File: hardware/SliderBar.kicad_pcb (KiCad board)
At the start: 2 copper layers, 36 parts, among them J1 USB_B_Mini, J2 MOTOR_OUT, J3 POT_IN, J4 DEBUG, U1 MIC5205-3.3YM5, U2 MT3608, U3 STM32F072C8Tx, U4 TB6612FNG

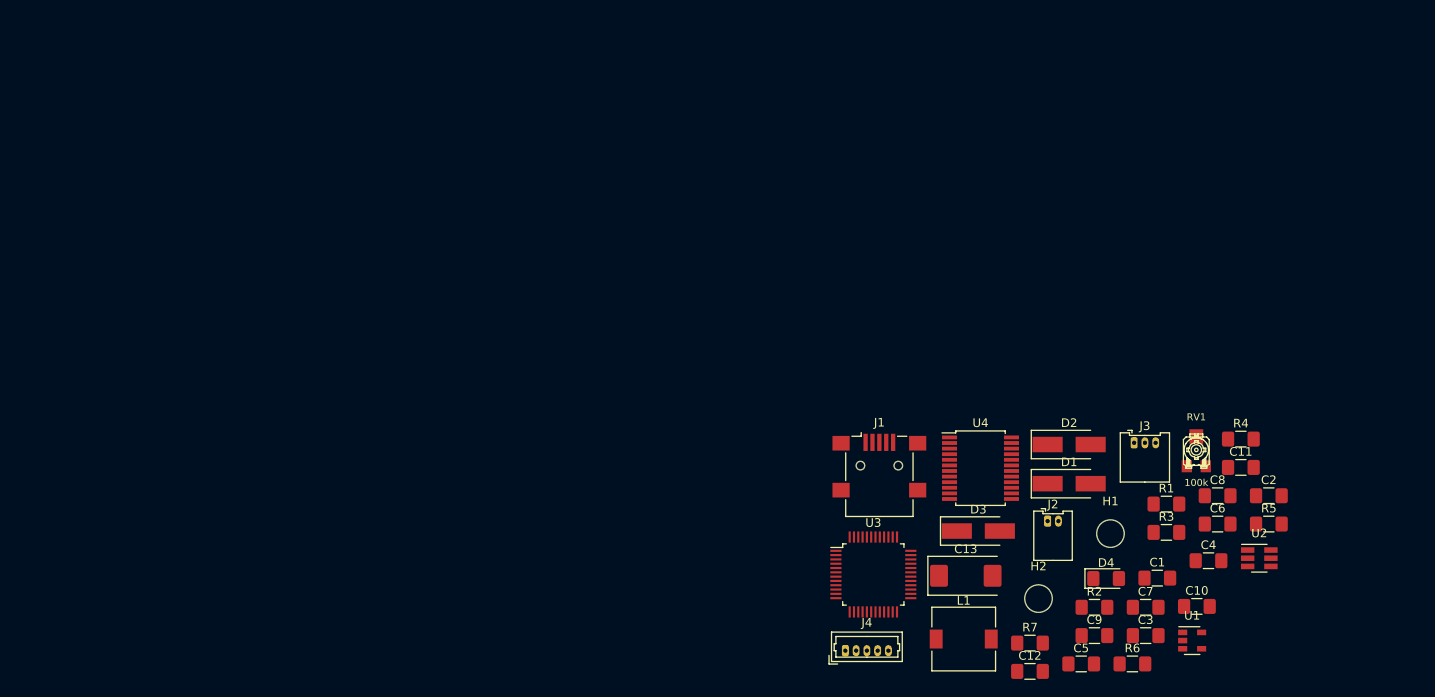
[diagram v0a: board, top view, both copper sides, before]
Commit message: Fix potentiometer wiring, move Nelib library outside of project
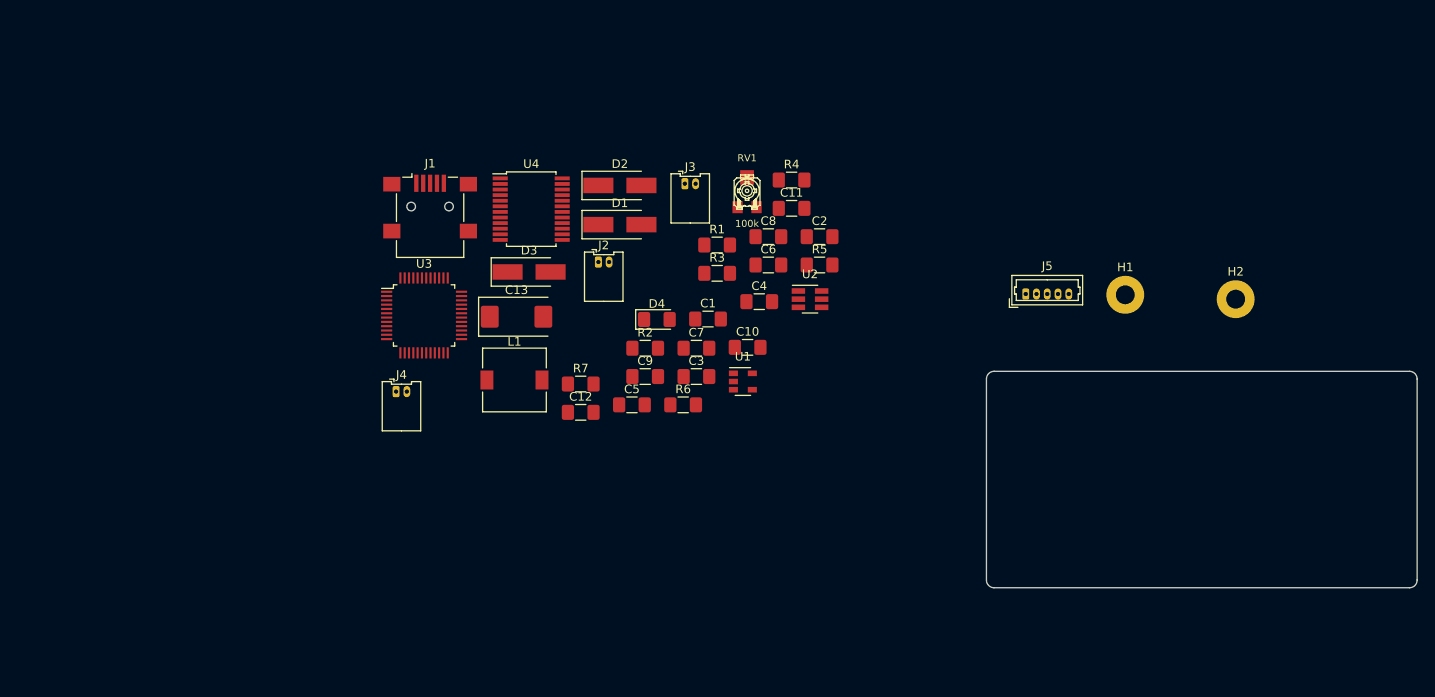
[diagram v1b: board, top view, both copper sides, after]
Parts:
- added J5: DEBUG, Connector_Molex:Molex_PicoBlade_53047-0510_1x05_P1.25mm_Vertical, F.Cu at (141.9, 46.9)
- H1, H2: footprint MountingHole:MountingHole_3.2mm_M3_ISO14580 -> MountingHole:MountingHole_2.2mm_M2_Pad
- J2: value MOTOR_OUT -> MOTOR
- J3: value POT_IN -> TAPER_RIGHT; footprint Connector_Molex:Molex_PicoBlade_53048-0310_1x03_P1.25mm_Horizontal -> Connector_Molex:Molex_PicoBlade_53048-0210_1x02_P1.25mm_Horizontal
- J4: value DEBUG -> TAPER_LEFT; footprint Connector_Molex:Molex_PicoBlade_53047-0510_1x05_P1.25mm_Vertical -> Connector_Molex:Molex_PicoBlade_53048-0210_1x02_P1.25mm_Horizontal
- moved R6 60.3 mm to (102.1, 59.8)
- moved C1 60.3 mm to (104.9, 49.8)
- moved C11 60.3 mm to (114.7, 36.9)
- moved C12 60.3 mm to (90.2, 60.6)
- moved C2 60.3 mm to (117.9, 40.2)
- moved C3 60.3 mm to (103.6, 56.5)
- moved C7 60.3 mm to (103.6, 53.2)
- moved D3 60.3 mm to (84.2, 44.3)
- moved D4 60.3 mm to (99.0, 49.9)
- moved J1 60.3 mm to (72.7, 36.7)
- moved J3 60.3 mm to (102.3, 34.1)
- moved J4 60.3 mm to (68.7, 58.2)
- moved R1 60.3 mm to (106.0, 41.2)
- moved R3 60.3 mm to (106.0, 44.5)
- moved R4 60.3 mm to (114.7, 33.7)
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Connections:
- J4 pad 1: SWDIO -> TOUCH_SENSE
- RV1 pad 2: Net-(RV1-Pad2) -> (no net)
- U3 pad 14: Net-(U3-Pad14) -> (no net)
- U3 pad 15: Net-(U3-Pad15) -> (no net)
- U3 pad 16: Net-(U3-Pad16) -> (no net)
- U3 pad 17: Net-(U3-Pad17) -> (no net)
- U3 pad 19: Net-(U3-Pad19) -> (no net)
- U3 pad 2: Net-(U3-Pad2) -> (no net)
- U3 pad 20: Net-(U3-Pad20) -> (no net)
- U3 pad 21: Net-(U3-Pad21) -> (no net)
- U3 pad 22: Net-(U3-Pad22) -> (no net)
- U3 pad 25: Net-(U3-Pad25) -> (no net)
- U3 pad 26: Net-(U3-Pad26) -> (no net)
- U3 pad 27: Net-(U3-Pad27) -> (no net)
- U3 pad 28: Net-(U3-Pad28) -> (no net)
- U3 pad 29: Net-(U3-Pad29) -> (no net)
- U3 pad 3: Net-(U3-Pad3) -> (no net)
- U3 pad 30: Net-(U3-Pad30) -> (no net)
- U3 pad 31: Net-(U3-Pad31) -> (no net)
- U3 pad 38: Net-(U3-Pad38) -> (no net)
- U3 pad 39: Net-(U3-Pad39) -> (no net)
- U3 pad 4: Net-(U3-Pad4) -> (no net)
- U3 pad 40: Net-(U3-Pad40) -> (no net)
- U3 pad 41: Net-(U3-Pad41) -> (no net)
- U3 pad 42: Net-(U3-Pad42) -> (no net)
- U3 pad 43: Net-(U3-Pad43) -> (no net)
- U3 pad 45: Net-(U3-Pad45) -> (no net)
- U3 pad 46: Net-(U3-Pad46) -> (no net)
- U3 pad 5: Net-(U3-Pad5) -> (no net)
- U3 pad 6: Net-(U3-Pad6) -> (no net)
- U4 pad 11: Net-(U4-Pad11) -> (no net)
- U4 pad 12: Net-(U4-Pad12) -> (no net)
- U4 pad 15: Net-(U4-Pad15) -> (no net)
- U4 pad 16: Net-(U4-Pad16) -> (no net)
- U4 pad 17: Net-(U4-Pad17) -> (no net)
- U4 pad 7: Net-(U4-Pad7) -> (no net)
- U4 pad 8: Net-(U4-Pad8) -> (no net)
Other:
- board outline added: 50 x 25.1 mm

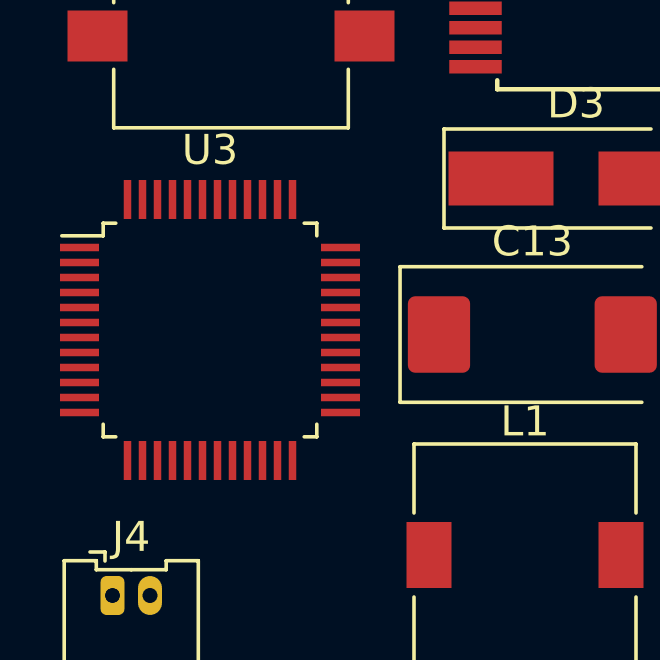
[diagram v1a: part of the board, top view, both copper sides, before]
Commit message: Add some 3D models from internet, fix some things
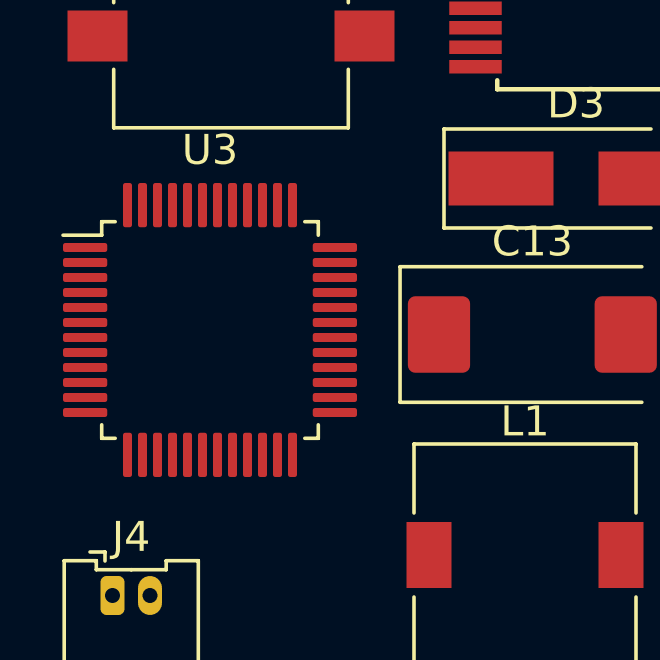
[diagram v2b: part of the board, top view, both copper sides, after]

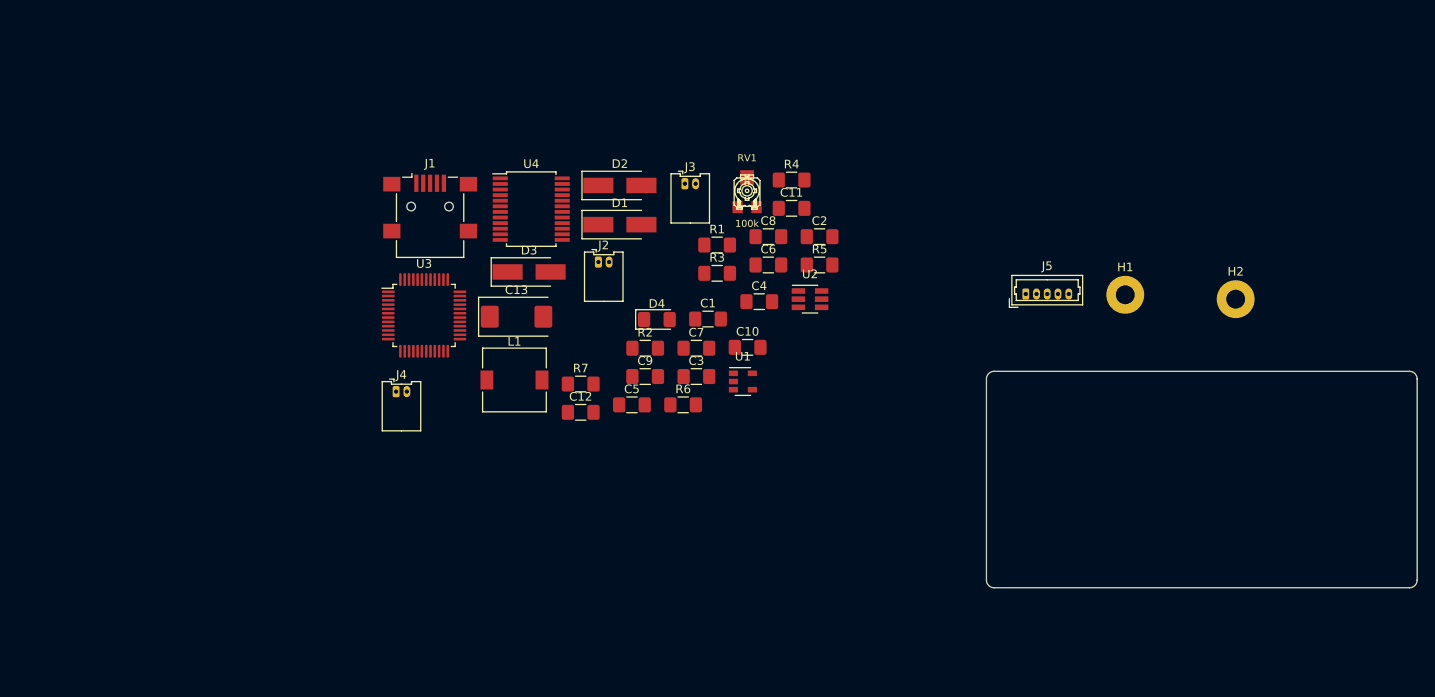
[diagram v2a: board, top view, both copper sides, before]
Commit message: Removed USB DP/DM resistors & Placed connectors
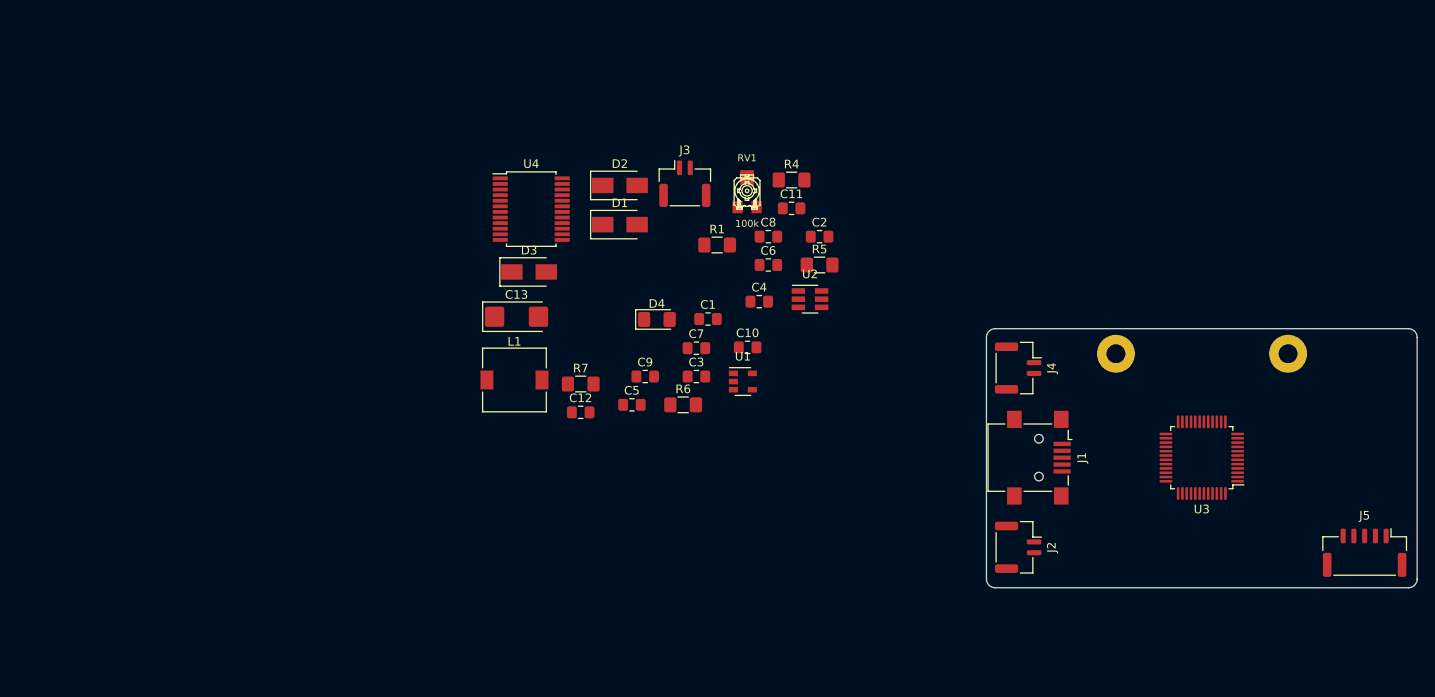
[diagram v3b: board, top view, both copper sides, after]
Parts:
- removed R2, R3: 20, Resistor_SMD:R_1206_3216Metric_Pad1.42x1.75mm_HandSolder
- C1, C10, C11, C2, C3, C4, C5, C6, C7, C8, C9: footprint Capacitor_SMD:C_1206_3216Metric_Pad1.42x1.75mm_HandSolder -> Capacitor_SMD:C_0805_2012Metric_Pad1.15x1.40mm_HandSolder
- C12: value 100nF -> 100n; footprint Capacitor_SMD:C_1206_3216Metric_Pad1.42x1.75mm_HandSolder -> Capacitor_SMD:C_0805_2012Metric_Pad1.15x1.40mm_HandSolder
- C13: footprint Capacitor_Tantalum_SMD:CP_EIA-7343-15_Kemet-W -> Capacitor_Tantalum_SMD:CP_EIA-6032-28_Kemet-C_Pad2.25x2.35mm_HandSolder
- D1, D2, D3: value 1N4001 -> STPS1L40; footprint Diode_SMD:D_SMA_Handsoldering -> Diode_SMD:D_SMA
- H1, H2: moved to B.Cu
- J2, J3, J4: footprint Connector_Molex:Molex_PicoBlade_53048-0210_1x02_P1.25mm_Horizontal -> Connector_JST:JST_GH_SM02B-GHS-TB_1x02-1MP_P1.25mm_Horizontal
- J5: footprint Connector_Molex:Molex_PicoBlade_53047-0510_1x05_P1.25mm_Vertical -> Connector_JST:JST_GH_BM05B-GHS-TBT_1x05-1MP_P1.25mm_Vertical
- moved U3 91.9 mm to (162.3, 65.9), turned to 180 degrees
- moved J1 76.5 mm to (143.4, 65.9), turned to 270 degrees
- moved J4 72.3 mm to (141.0, 55.5), turned to 270 degrees
- moved J2 59.0 mm to (141.0, 76.3), turned to 270 degrees
- moved J5 49.5 mm to (181.2, 77.0), turned to 180 degrees
- moved H2 8.79 mm to (172.3, 53.8)
- moved H1 6.94 mm to (152.3, 53.8)
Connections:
- J1 pad 2: /D- -> USB_DN
- J1 pad 3: /D+ -> USB_DP
- RV1 pad 1: +10V -> (no net)
- RV1 pad 2: (no net) -> Net-(R5-Pad2)
- RV1 pad 3: Net-(R5-Pad2) -> +10V
- U3 pad 19: (no net) -> TOUCH_SENSE
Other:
- board size 50 x 25.1 mm -> 50 x 30.1 mm

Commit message: Placed some components, fixed schematic
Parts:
- removed R6: 1k, Resistor_SMD:R_1206_3216Metric_Pad1.42x1.75mm_HandSolder
- removed R7: 10k, Resistor_SMD:R_1206_3216Metric_Pad1.42x1.75mm_HandSolder
- added R2: 1.5k, Resistor_SMD:R_0805_2012Metric_Pad1.15x1.40mm_HandSolder, F.Cu at (150.4, 68.6)
- added R3: 3k, Resistor_SMD:R_0805_2012Metric_Pad1.15x1.40mm_HandSolder, F.Cu at (28.7, 62.7)
- R1: footprint Resistor_SMD:R_1206_3216Metric_Pad1.42x1.75mm_HandSolder -> Resistor_SMD:R_0805_2012Metric_Pad1.15x1.40mm_HandSolder
- R4: value 1.5k -> 1k; footprint Resistor_SMD:R_1206_3216Metric_Pad1.42x1.75mm_HandSolder -> Resistor_SMD:R_0805_2012Metric_Pad1.15x1.40mm_HandSolder
- R5: value 3k -> 10k; footprint Resistor_SMD:R_1206_3216Metric_Pad1.42x1.75mm_HandSolder -> Resistor_SMD:R_0805_2012Metric_Pad1.15x1.40mm_HandSolder
- moved D3 88.2 mm to (172.0, 36.2)
- moved J3 83.7 mm to (183.1, 55.5), turned to 90 degrees
- moved C3 79.6 mm to (180.5, 77.0)
- moved C1 79.2 mm to (26.3, 59.2)
- moved D2 77.8 mm to (172.1, 42.0)
- moved RV1 73.3 mm to (43.4, 66.8)
- moved C9 73.3 mm to (170.6, 64.3)
- moved U1 73.3 mm to (180.5, 73.2), turned to 180 degrees
- moved C4 69.9 mm to (176.0, 73.1), turned to 270 degrees
- moved C5 69.1 mm to (27.6, 68.3)
- moved C2 69.0 mm to (180.5, 69.3), turned to 180 degrees
- moved D1 65.9 mm to (35.4, 67.7)
- moved C8 64.4 mm to (170.6, 66.9)
- moved C10 63.2 mm to (170.6, 69.6)
- moved C11 59.0 mm to (173.2, 30.1)
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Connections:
- R4 pad 1: +3V3 -> +5V
- R4 pad 2: USB_DP -> Net-(D4-Pad2)
- R5 pad 1: GND -> Net-(R5-Pad1)
- R5 pad 2: Net-(R5-Pad2) -> GND
- RV1 pad 2: Net-(R5-Pad2) -> Net-(R3-Pad2)
- U2 pad 3: Net-(R5-Pad2) -> Net-(R3-Pad2)
- U3 pad 44: Net-(R7-Pad1) -> Net-(R5-Pad1)
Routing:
- net USB_DN: track 0.00 -> 12.8 mm
- net USB_DP: track 0.00 -> 12.6 mm
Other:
- net class Default: trace_width 0.1524 -> 0.2032
- net class PowerLowVoltage: trace_width 0.381 -> 0.4064

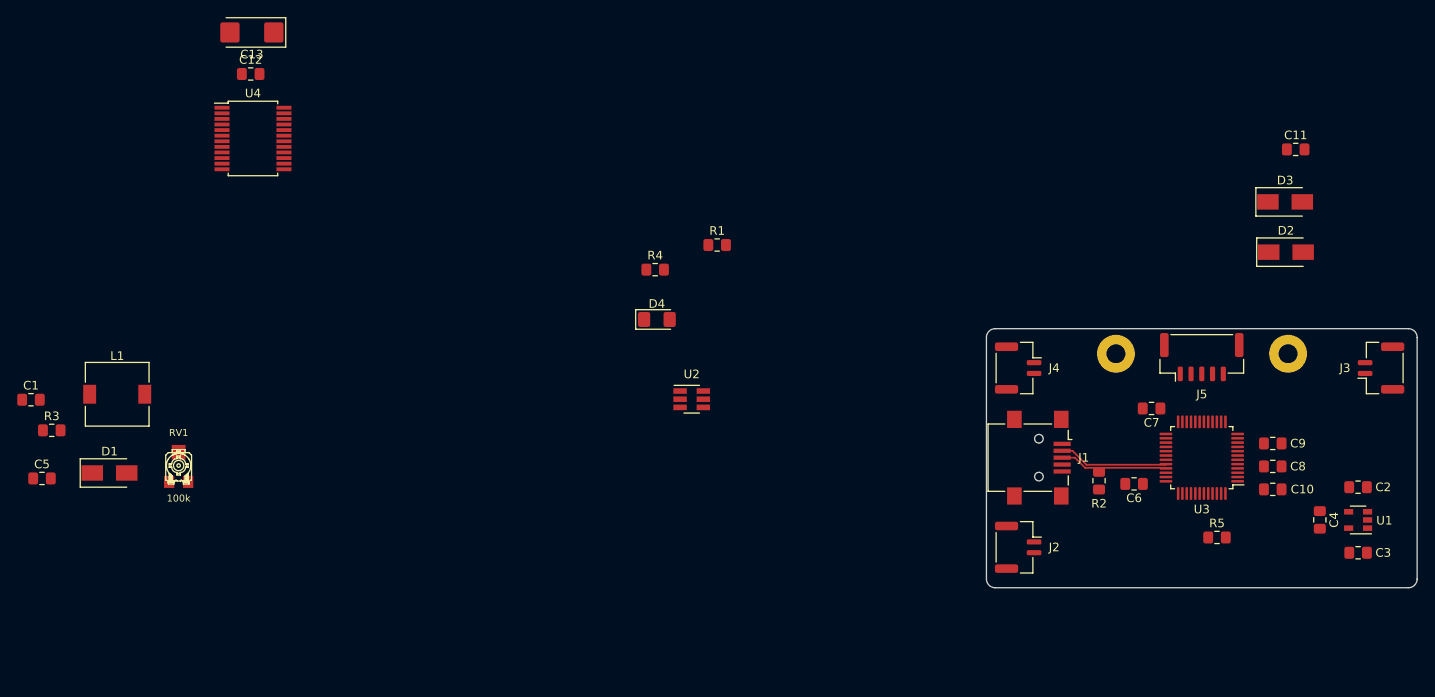
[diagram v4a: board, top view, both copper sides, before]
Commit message: Placed front components
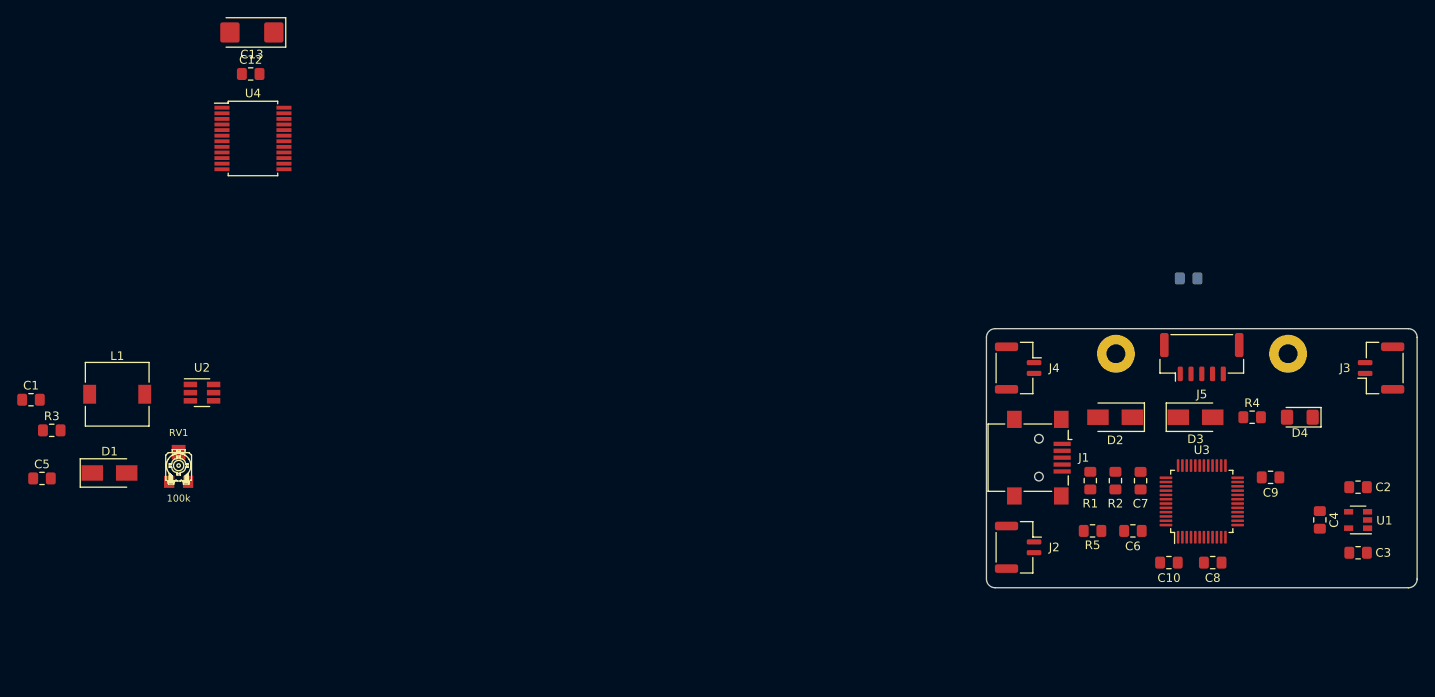
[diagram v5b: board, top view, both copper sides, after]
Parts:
- C11: moved to B.Cu
- moved D4 75.6 mm to (173.7, 61.2), turned to 180 degrees
- moved R4 71.4 mm to (168.2, 61.2)
- moved U2 56.9 mm to (46.1, 58.4)
- moved R1 51.3 mm to (149.4, 68.6), turned to 270 degrees
- moved D2 27.6 mm to (152.2, 61.2), turned to 180 degrees
- moved D3 27.1 mm to (161.6, 61.2)
- moved C11 19.5 mm to (160.8, 45.1)
- moved C10 14.8 mm to (158.5, 78.1), turned to 180 degrees
- moved R5 14.5 mm to (149.6, 74.4), turned to 180 degrees
- moved C8 13.2 mm to (163.6, 78.1)
- moved C7 8.49 mm to (155.2, 68.6), turned to 270 degrees
- moved C6 5.46 mm to (154.3, 74.4)
- moved U3 5.08 mm to (162.3, 71.0), turned to 90 degrees
- moved C9 3.95 mm to (170.3, 68.2)
- moved R2 1.91 mm to (152.3, 68.6)
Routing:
- net USB_DN: track 12.8 -> 0.00 mm
- net USB_DP: track 12.6 -> 0.00 mm

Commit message: Placed back components
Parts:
- C1, C12, C13, C5, D1, J2, J3, J4, L1, R3, RV1, U2, U4: moved to B.Cu
- moved C1 153.1 mm to (179.3, 62.1), turned to 90 degrees
- moved R3 140.9 mm to (169.5, 62.6), turned to 90 degrees
- moved L1 140.3 mm to (176.0, 71.0)
- moved C5 138.4 mm to (166.0, 66.4), turned to 270 degrees
- moved D1 131.7 mm to (167.0, 71.0)
- moved U2 128.9 mm to (174.9, 64.0)
- moved RV1 118.6 mm to (162.0, 63.4), turned to 180 degrees
- moved C12 112.1 mm to (153.5, 68.5), turned to 180 degrees
- moved C13 110.2 mm to (151.1, 64.6)
- moved U4 109.3 mm to (151.1, 74.9)
- moved C11 13.5 mm to (157.9, 58.3)
- turned J2 to 90 degrees
- turned J3 to 270 degrees
- turned J4 to 90 degrees
